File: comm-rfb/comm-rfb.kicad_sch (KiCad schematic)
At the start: 5 parts, among them J1 PC104_Connector

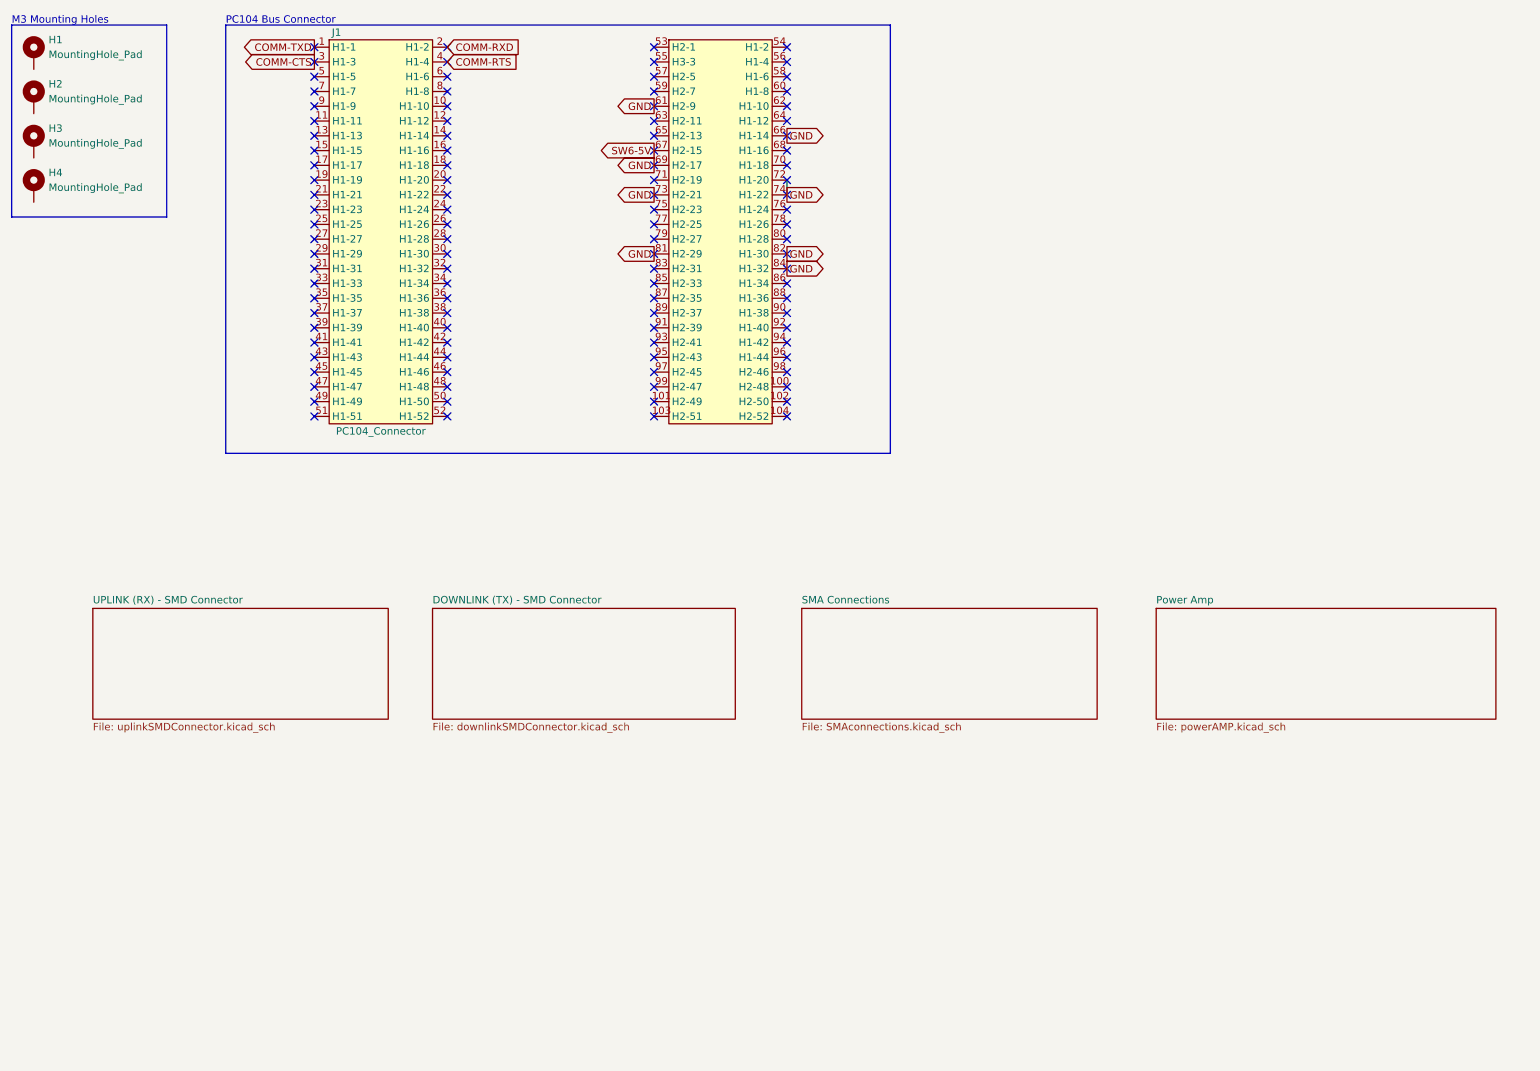
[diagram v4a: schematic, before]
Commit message: added mcu connections
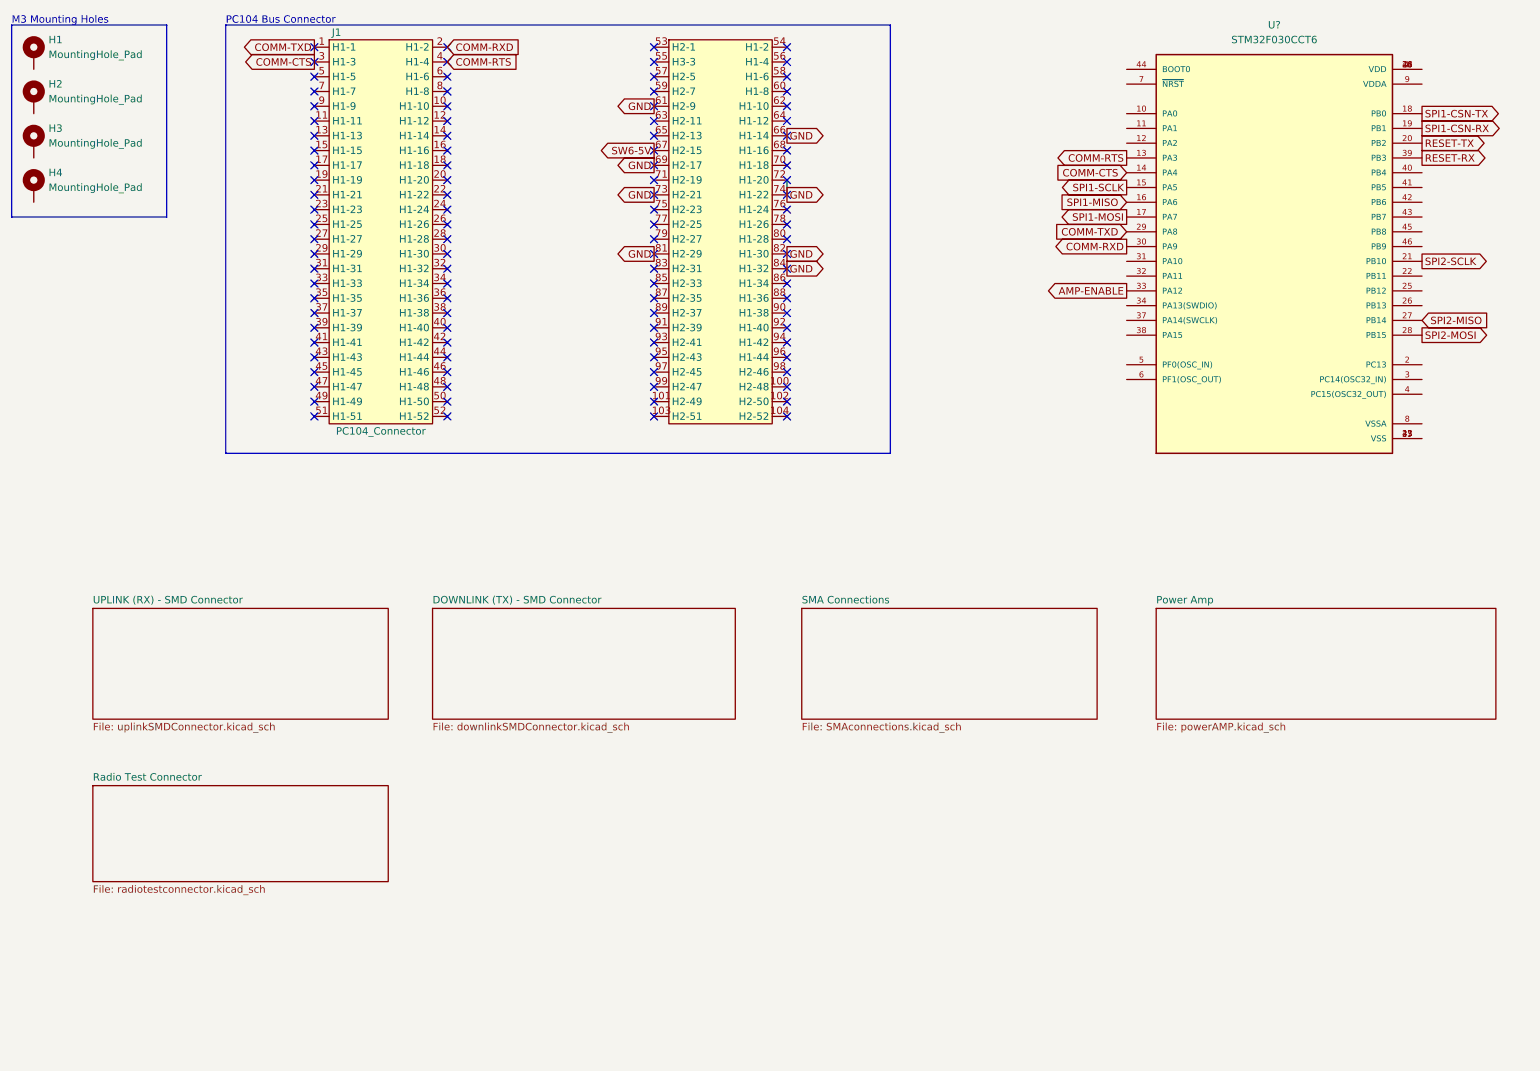
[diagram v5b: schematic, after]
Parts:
- added U?: STM32F030CCT6, QFP50P900X900X160-48N, symbol STM32F030CCT6:STM32F030CCT6
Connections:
- net COMM-CTS: now also U?.14 (PA4)
- net COMM-RTS: now also U?.13 (PA3)
- net COMM-RXD: now also U?.30 (PA9)
- net COMM-TXD: now also U?.29 (PA8)
- new net: U?.1 (VDD), U?.24 (VDD), U?.36 (VDD), U?.48 (VDD)
- new net: U?.23 (VSS), U?.35 (VSS), U?.47 (VSS)
- new net AMP-ENABLE: U?.33 (PA12)
- new net RESET-RX: U?.39 (PB3)
- new net RESET-TX: U?.20 (PB2)
- new net SPI1-CSN-RX: U?.19 (PB1)
- new net SPI1-CSN-TX: U?.18 (PB0)
- new net SPI1-MISO: U?.16 (PA6)
- new net SPI1-MOSI: U?.17 (PA7)
- new net SPI1-SCLK: U?.15 (PA5)
- new net SPI2-MISO: U?.27 (PB14)
- new net SPI2-MOSI: U?.28 (PB15)
- new net SPI2-SCLK: U?.21 (PB10)
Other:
- added sheet Radio Test Connector (radiotestconnector.kicad_sch)
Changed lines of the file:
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@@
     (effects (font (size 1.27 1.27)) (justify left bottom))
   )
+  (global_label "SPI1-MOSI" (shape output) (at 205.74 48.26 180) (fields_autoplaced)
+    (effects (font (size 1.27 1.27)) (justify right))
+    (property "Intersheet References" "${INTERSHEET_REFS}" (id 0) (at 192.8645 48.1806 0)
+      (effects (font (size 1.27 1.27)) (justify right) hide)
+    )
+  )
+  (global_label "COMM-RXD" (shape output) (at 205.74 53.34 180) (fields_autoplaced)
+    (effects (font (size 1.27 1.27)) (justify right))
+    (property "Intersheet References" "${INTERSHEET_REFS}" (id 0) (at 192.5017 53.2606 0)
+      (effects (font (size 1.27 1.27)) (justify right) hide)
+    )
+  )
+  (global_label "RESET-TX" (shape output) (at 256.54 35.56 0) (fields_autoplaced)
+    (effects (font (size 1.27 1.27)) (justify left))
+    (property "Intersheet References" "${INTERSHEET_REFS}" (id 0) (at 268.4479 35.4806 0)
+      (effects (font (size 1.27 1.27)) (justify left) hide)
+    )
+  )
   (global_label "GND" (shape output) (at 124.46 39.37 180) (fields_autoplaced)
     (effects (font (size 1.27 1.27)) (justify right))
@@
     )
   )
+  (global_label "COMM-TXD" (shape input) (at 205.74 50.8 180) (fields_autoplaced)
+    (effects (font (size 1.27 1.27)) (justify right))
+    (property "Intersheet References" "${INTERSHEET_REFS}" (id 0) (at 192.804 50.7206 0)
+      (effects (font (size 1.27 1.27)) (justify right) hide)
+    )
+  )
   (global_label "GND" (shape output) (at 147.32 44.45 0) (fields_autoplaced)
     (effects (font (size 1.27 1.27)) (justify left))
@@
     )
   )
+  (global_label "AMP-ENABLE" (shape output) (at 205.74 60.96 180) (fields_autoplaced)
+    (effects (font (size 1.27 1.27)) (justify right))
+    (property "Intersheet References" "${INTERSHEET_REFS}" (id 0) (at 190.9293 60.8806 0)
+      (effects (font (size 1.27 1.27)) (justify right) hide)
+    )
+  )
+  (global_label "SPI2-SCLK" (shape output) (at 256.54 55.88 0) (fields_autoplaced)
+    (effects (font (size 1.27 1.27)) (justify left))
+    (property "Intersheet References" "${INTERSHEET_REFS}" (id 0) (at 269.5969 55.8006 0)
+      (effects (font (size 1.27 1.27)) (justify left) hide)
+    )
+  )
   (global_label "GND" (shape output) (at 147.32 34.29 0) (fields_autoplaced)
     (effects (font (size 1.27 1.27)) (justify left))
@@
     )
   )
+  (global_label "SPI2-MISO" (shape input) (at 256.54 66.04 0) (fields_autoplaced)
+    (effects (font (size 1.27 1.27)) (justify left))
+    (property "Intersheet References" "${INTERSHEET_REFS}" (id 0) (at 269.4155 65.9606 0)
+      (effects (font (size 1.27 1.27)) (justify left) hide)
+    )
+  )
+  (global_label "SPI1-SCLK" (shape output) (at 205.74 43.18 180) (fields_autoplaced)
+    (effects (font (size 1.27 1.27)) (justify right))
+    (property "Intersheet References" "${INTERSHEET_REFS}" (id 0) (at 192.6831 43.1006 0)
+      (effects (font (size 1.27 1.27)) (justify right) hide)
+    )
+  )
+  (global_label "RESET-RX" (shape output) (at 256.54 38.1 0) (fields_autoplaced)
+    (effects (font (size 1.27 1.27)) (justify left))
+    (property "Intersheet References" "${INTERSHEET_REFS}" (id 0) (at 268.7502 38.0206 0)
+      (effects (font (size 1.27 1.27)) (justify left) hide)
+    )
+  )
   (global_label "SW6-5V" (shape output) (at 124.46 36.83 180) (fields_autoplaced)
     (effects (font (size 1.27 1.27)) (justify right))
@@
     )
   )
+  (global_label "SPI1-CSN-TX" (shape output) (at 256.54 30.48 0) (fields_autoplaced)
+    (effects (font (size 1.27 1.27)) (justify left))
+    (property "Intersheet References" "${INTERSHEET_REFS}" (id 0) (at 272.3788 30.4006 0)
+      (effects (font (size 1.27 1.27)) (justify left) hide)
+    )
+  )
   (global_label "GND" (shape output) (at 124.46 29.21 180) (fields_autoplaced)
     (effects (font (size 1.27 1.27)) (justify right))
@@
     )
   )
+  (global_label "SPI1-CSN-RX" (shape output) (at 256.54 33.02 0) (fields_autoplaced)
+    (effects (font (size 1.27 1.27)) (justify left))
+    (property "Intersheet References" "${INTERSHEET_REFS}" (id 0) (at 272.6812 32.9406 0)
+      (effects (font (size 1.27 1.27)) (justify left) hide)
+    )
+  )
   (global_label "GND" (shape output) (at 124.46 44.45 180) (fields_autoplaced)
     (effects (font (size 1.27 1.27)) (justify right))
     (property "Intersheet References" "${INTERSHEET_REFS}" (id 0) (at 118.1764 44.3706 0)
       (effects (font (size 1.27 1.27)) (justify right) hide)
+    )
+  )
+  (global_label "COMM-RTS" (shape output) (at 205.74 38.1 180) (fields_autoplaced)
+    (effects (font (size 1.27 1.27)) (justify right))
+    (property "Intersheet References" "${INTERSHEET_REFS}" (id 0) (at 192.804 38.0206 0)
+      (effects (font (size 1.27 1.27)) (justify right) hide)
+    )
+  )
+  (global_label "SPI1-MISO" (shape input) (at 205.74 45.72 180) (fields_autoplaced)
+    (effects (font (size 1.27 1.27)) (justify right))
+    (property "Intersheet References" "${INTERSHEET_REFS}" (id 0) (at 192.8645 45.6406 0)
+      (effects (font (size 1.27 1.27)) (justify right) hide)
+    )
+  )
+  (global_label "COMM-CTS" (shape input) (at 205.74 40.64 180) (fields_autoplaced)
+    (effects (font (size 1.27 1.27)) (justify right))
+    (property "Intersheet References" "${INTERSHEET_REFS}" (id 0) (at 192.804 40.5606 0)
+      (effects (font (size 1.27 1.27)) (justify right) hide)
+    )
+  )
+  (global_label "SPI2-MOSI" (shape output) (at 256.54 68.58 0) (fields_autoplaced)
+    (effects (font (size 1.27 1.27)) (justify left))
+    (property "Intersheet References" "${INTERSHEET_REFS}" (id 0) (at 269.4155 68.5006 0)
+      (effects (font (size 1.27 1.27)) (justify left) hide)
     )
   )
@@
     )
     (pin "1")
+  )
+  (symbol (lib_id "STM32F030CCT6:STM32F030CCT6") (at 231.14 53.34 0) (unit 1)
+    (in_bom yes) (on_board yes) (fields_autoplaced)
+    (property "Reference" "U?" (id 0) (at 231.14 15.24 0))
+    (property "Value" "STM32F030CCT6" (id 1) (at 231.14 17.78 0))
+    (property "Footprint" "QFP50P900X900X160-48N" (id 2) (at 231.14 53.34 0)
+      (effects (font (size 1.27 1.27)) (justify bottom) hide)
+    )
+    (property "Datasheet" "" (id 3) (at 231.14 53.34 0)
+      (effects (font (size 1.27 1.27)) hide)
+    )
+    (property "MANUFACTURER" "STMicroelectronics" (id 4) (at 231.14 53.34 0)
+      (effects (font (size 1.27 1.27)) (justify bottom) hide)
+    )
+    (pin "1")
+    (pin "10")
+    (pin "11")
+    (pin "12")
+    (pin "13")
+    (pin "14")
+    (pin "15")
+    (pin "16")
+    (pin "17")
+    (pin "18")
+    (pin "19")
+    (pin "2")
+    (pin "20")
+    (pin "21")
+    (pin "22")
+    (pin "23")
+    (pin "24")
+    (pin "25")
+    (pin "26")
+    (pin "27")
+    (pin "28")
+    (pin "29")
+    (pin "3")
+    (pin "30")
+    (pin "31")
+    (pin "32")
+    (pin "33")
+    (pin "34")
+    (pin "35")
+    (pin "36")
+    (pin "37")
+    (pin "38")
+    (pin "39")
+    (pin "4")
+    (pin "40")
+    (pin "41")
+    (pin "42")
+    (pin "43")
+    (pin "44")
+    (pin "45")
+    (pin "46")
+    (pin "47")
+    (pin "48")
+    (pin "5")
+    (pin "6")
+    (pin "7")
+    (pin "8")
+    (pin "9")
   )
   (symbol (lib_id "qset-connector-library:PC104_Connector") (at 106.68 15.24 0) (unit 1)
@@
     )
   )
+  (sheet (at 27.94 146.05) (size 50.8 16.51) (fields_autoplaced)
+    (stroke (width 0.1524) (type solid) (color 0 0 0 0))
+    (fill (color 0 0 0 0.0000))
+    (property "Sheet name" "Radio Test Connector" (id 0) (at 27.94 145.3384 0)
+      (effects (font (size 1.27 1.27)) (justify left bottom))
+    )
+    (property "Sheet file" "radiotestconnector.kicad_sch" (id 1) (at 27.94 163.1446 0)
+      (effects (font (size 1.27 1.27)) (justify left top))
+    )
+  )
   (sheet_instances
     (path "/" (page "1"))
@@
     (path "/1134daf0-036a-4c8a-b49c-c0c69387f2ca" (page "4"))
     (path "/692e9f18-86ea-4b4e-8432-aeb1e884c0b2" (page "5"))
+    (path "/87e579cb-6bd6-444c-8886-91b899b8cce6" (page "6"))
   )
   (symbol_instances
@@
       (reference "R?") (unit 1) (value "9.1k") (footprint "")
     )
+    (path "/b80cbbdc-16b1-4161-95f2-05a8bd9b42d9"
+      (reference "U?") (unit 1) (value "STM32F030CCT6") (footprint "QFP50P900X900X160-48N")
+    )
     (path "/692e9f18-86ea-4b4e-8432-aeb1e884c0b2/c90ac0f1-4a37-4b59-9cdb-77baf606bb78"
